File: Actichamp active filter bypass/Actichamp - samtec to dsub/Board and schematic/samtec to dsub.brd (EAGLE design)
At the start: 73 x 39 mm, 2 parts

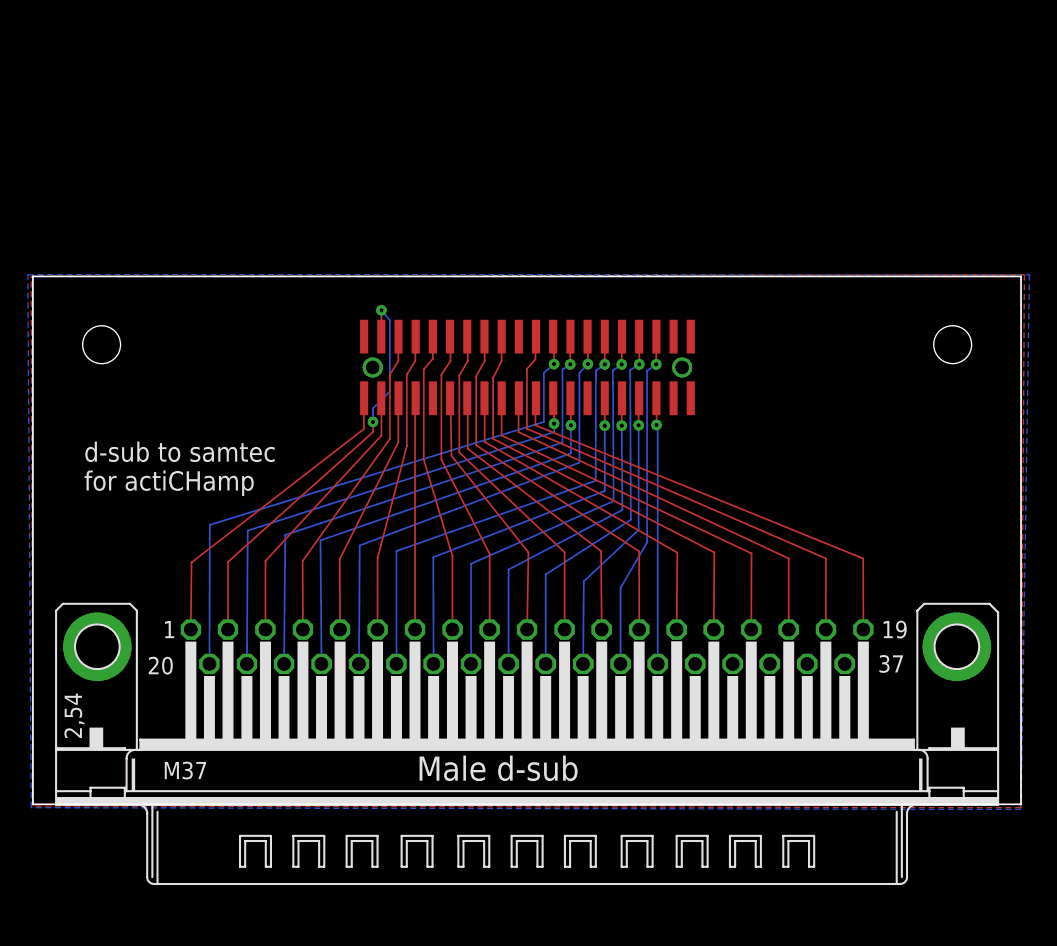
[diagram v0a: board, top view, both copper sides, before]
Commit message: updated Dsub to Actichamp connector board. PCBWAY gerbers
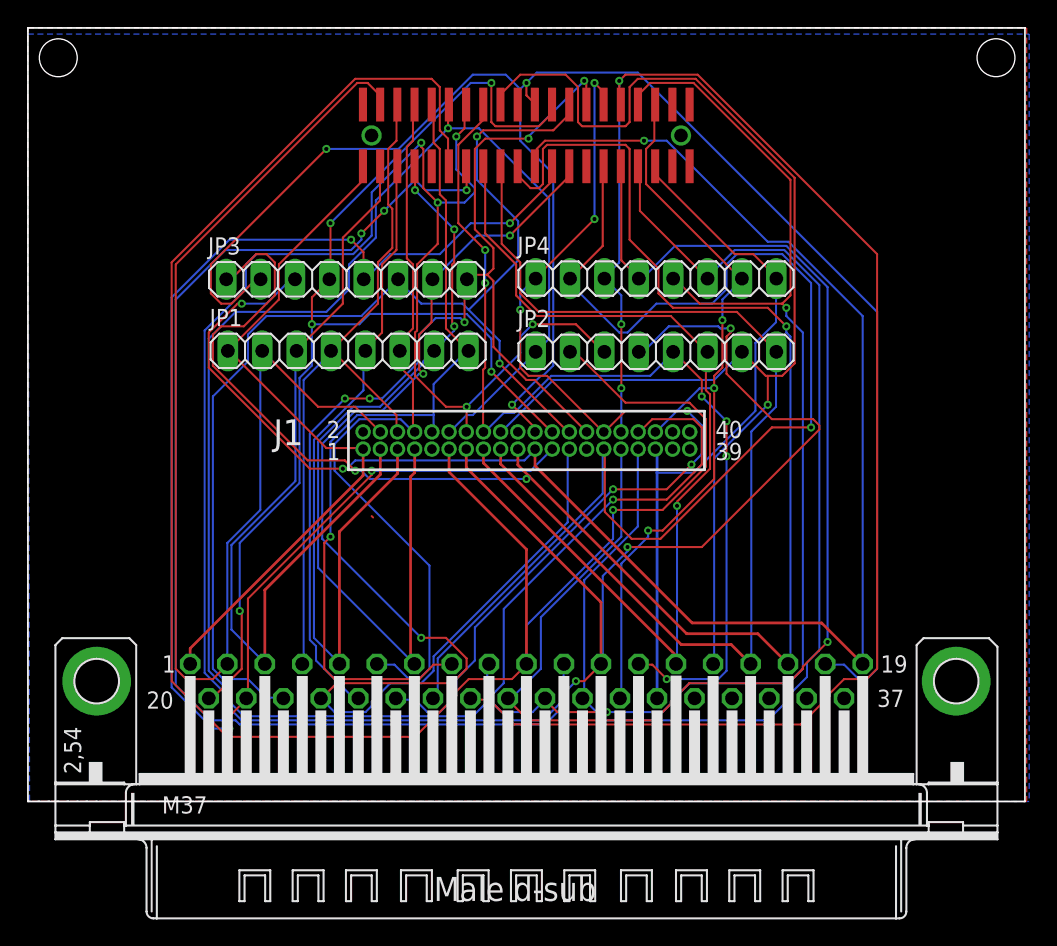
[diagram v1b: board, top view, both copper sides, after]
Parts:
- removed U$1: SAMTEC_FTSH_LARGEPAD, mayo:SAMTEC-FTSH-LARGEPAD
- added J1: SAMTEC-FTSH-120-01-X-DJ, SAMTEC-FTSH-120-01-X-D:SAMTEC-FTSH-120-01-X-D
- added JP1, JP2, JP3, JP4: (no value), pinhead:1X08
- added U$2: SAMTEC-FTSH-120-01-F-DV-A, samtec to dsub:SAMTEC-FTSH-LARGEPAD
- moved X1 2.54 mm to (61.0, 38.1)
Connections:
- net CH1: now also J1.1, JP1.1, U$2.P$1; no longer U$1.P$21
- net CH10: now also J1.11, JP2.2, U$2.P$11; no longer U$1.P$26
- net CH11: now also J1.14, JP2.3, U$2.P$14; no longer U$1.P$7
- net CH12: now also J1.13, JP2.4, U$2.P$13; no longer U$1.P$27
- net CH13: now also J1.16, JP2.5, U$2.P$16; no longer U$1.P$8
- net CH14: now also J1.15, JP2.6, U$2.P$15; no longer U$1.P$28
- net CH15: now also J1.18, JP2.7, U$2.P$18; no longer U$1.P$9
- net CH16: now also J1.17, JP2.8, U$2.P$17; no longer U$1.P$29
- net CH17: now also J1.19, JP3.1, U$2.P$19; no longer U$1.P$30
- net CH18: now also J1.22, JP3.2, U$2.P$22; no longer U$1.P$11
- net CH19: now also J1.21, JP3.3, U$2.P$21; no longer U$1.P$31
- net CH2: now also J1.4, JP1.2, U$2.P$4; no longer U$1.P$2
- net CH20: now also J1.24, JP3.4, U$2.P$24; no longer U$1.P$12
- net CH21: now also J1.23, JP3.5, U$2.P$23; no longer U$1.P$32
- net CH22: now also J1.26, JP3.6, U$2.P$26; no longer U$1.P$13
- net CH23: now also J1.25, JP3.7, U$2.P$25; no longer U$1.P$33
- net CH24: now also J1.28, JP3.8, U$2.P$28; no longer U$1.P$14
- net CH25: now also J1.30, JP4.1, U$2.P$30; no longer U$1.P$15
- net CH26: now also J1.29, JP4.2, U$2.P$29; no longer U$1.P$35
- net CH27: now also J1.32, JP4.3, U$2.P$32; no longer U$1.P$16
- net CH28: now also J1.31, JP4.4, U$2.P$31; no longer U$1.P$36
- net CH29: now also J1.34, JP4.5, U$2.P$34; no longer U$1.P$17
- net CH3: now also J1.3, JP1.3, U$2.P$3; no longer U$1.P$22
- net CH30: now also J1.33, JP4.6, U$2.P$33; no longer U$1.P$37
- net CH31: now also J1.36, JP4.7, U$2.P$36; no longer U$1.P$18
- net CH32: now also J1.35, JP4.8, U$2.P$35; no longer U$1.P$38
- net CH4: now also J1.6, JP1.4, U$2.P$6; no longer U$1.P$3
- net CH5: now also J1.5, JP1.5, U$2.P$5; no longer U$1.P$23
- net CH6: now also J1.8, JP1.6, U$2.P$8; no longer U$1.P$4
- net CH7: now also J1.7, JP1.7, U$2.P$7; no longer U$1.P$24
- net CH8: now also J1.10, JP1.8, U$2.P$10; no longer U$1.P$5
- net CH9: now also J1.12, JP2.1, U$2.P$12; no longer U$1.P$6
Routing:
- net CH12: track 22.0 -> 158.0 mm, vias 0 -> 6
- net CH10: track 19.1 -> 149.2 mm, vias 0 -> 1
- net CH11: track 25.2 -> 131.4 mm, vias 0 -> 5
- net CH17: track 29.8 -> 128.7 mm, vias 0 -> 3
- net CH18: track 36.4 -> 131.5 mm, vias 0 -> 3
- net CH19: track 33.4 -> 126.7 mm, vias 0 -> 3
- net CH29: track 28.0 -> 121.1 mm, vias 1 -> 3
- net CH9: track 22.7 -> 109.1 mm, vias 0 -> 1
- net CH27: track 31.4 -> 116.8 mm, vias 1 -> 3
- net CH28: track 24.7 -> 100.3 mm
- net CH21: track 36.1 -> 108.1 mm, vias 1 -> 4
- net CH30: track 21.4 -> 88.9 mm, vias 1 -> 0
- net CH26: track 28.3 -> 91.9 mm
- net CH23: track 32.8 -> 95.6 mm, vias 1 -> 3
- net CH15: track 31.8 -> 94.1 mm, vias 0 -> 1
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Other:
- board size 73 x 39 mm -> 73.7 x 57.1 mm
- board text added: "1"
- board text added: "17"
